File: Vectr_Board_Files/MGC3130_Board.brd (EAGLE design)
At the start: 146.5 x 107 mm, 112 parts, among them U101 MCP1755S, U102 MGC3130, U201 74HCT595BQ,115, U202 74HCT595BQ,115, U203 74HCT595BQ,115

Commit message: Preliminary Final Revision
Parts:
- moved R109 6.02 mm to (4.88, 53.9)
- flipped TO_MAIN to the bottom
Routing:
- net LED_PWM_4: track 236.8 -> 211.8 mm, vias 3 -> 4
- net GND: track 196.1 -> 217.4 mm, vias 11 -> 13
- net 5V: track 83.4 -> 99.9 mm
- net AGND: track 32.5 -> 48.0 mm
- net 3.3V: track 133.3 -> 120.3 mm
- net N$92: track 461.9 -> 473.4 mm, vias 17 -> 14
- net I2C1_SDA: track 103.4 -> 94.8 mm
- net LED_PWM_3: track 30.3 -> 38.7 mm, vias 0 -> 2
- net LED_PWM_1: track 63.8 -> 67.8 mm
- net MGC3130_IRQ: track 91.9 -> 94.8 mm, vias 0 -> 1
- net LED_PWM_2: track 82.4 -> 84.9 mm
- net SR_CLK: track 272.4 -> 270.4 mm, vias 7 -> 4
- net MGC3130_RESET: track 117.2 -> 115.3 mm
- net N$77: track 185.4 -> 187.2 mm
- net N$69: track 204.1 -> 205.8 mm
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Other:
- board text added: "VECTR HACKME ELECTRONICS REV 1.2"
- board text removed: "The connector is at 5.5 and 44.25"
- board text removed: "VECTR HACKME ELECTRONICS REV 1.1"

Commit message: Correcting the board files to match original production Vectr
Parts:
- TO_MAIN: value 16-SMT -> M50-3601042; device HackMe:16-SMT -> HackMe:M50-3601042
- moved R231 144.1 mm to (145.3, 8.08), flipped to the top
- moved R207 142.5 mm to (144.5, 102.0), flipped to the top
- moved T205 142.3 mm to (144.4, 4.74), flipped to the top
- moved C203 141.2 mm to (143.8, 17.6), flipped to the top
- moved T201 141.0 mm to (2.76, 92.4), flipped to the top
- moved C201 139.6 mm to (3.43, 11.9), flipped to the top
- moved R239 139.5 mm to (3.48, 60.0), flipped to the bottom
- moved R238 139.0 mm to (3.73, 75.4), flipped to the bottom
- moved R210 139.0 mm to (3.74, 68.0), flipped to the bottom
- moved R223 139.0 mm to (3.74, 44.8), flipped to the bottom
- moved R211 138.9 mm to (3.79, 83.5), flipped to the bottom
- moved R208 138.8 mm to (3.84, 36.7), flipped to the bottom
- moved R209 138.8 mm to (3.84, 52.4), flipped to the bottom
- moved R224 138.8 mm to (3.84, 29.3), flipped to the bottom
- moved R222 138.8 mm to (3.85, 21.5), flipped to the bottom
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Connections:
- net 5V: now also TO_MAIN.1, TO_MAIN.20; no longer TO_MAIN.P$1, TO_MAIN.P$2
- net AGND: now also TO_MAIN.11; no longer TO_MAIN.P$16
- net GND: now also TO_MAIN.10; no longer TO_MAIN.P$15
- net I2C1_SCL: now also TO_MAIN.2; no longer TO_MAIN.P$3
- net I2C1_SDA: now also TO_MAIN.19; no longer TO_MAIN.P$4
- net LED_PWM_1: now also TO_MAIN.5; no longer TO_MAIN.P$9
- net LED_PWM_2: now also TO_MAIN.16; no longer TO_MAIN.P$10
- net LED_PWM_3: now also TO_MAIN.6; no longer TO_MAIN.P$11
- net LED_PWM_4: now also TO_MAIN.15; no longer TO_MAIN.P$12
- net LED_PWM_5: now also TO_MAIN.7; no longer TO_MAIN.P$13
- net MGC3130_IRQ: now also TO_MAIN.18; no longer TO_MAIN.P$6
- net MGC3130_RESET: now also TO_MAIN.3; no longer TO_MAIN.P$5
- net SR_CLK: now also TO_MAIN.17; no longer TO_MAIN.P$8
- net SR_DATA: now also TO_MAIN.4; no longer TO_MAIN.P$7
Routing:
- net LED_PWM_4: track 211.8 -> 238.1 mm, vias 4 -> 3
- net GND: track 217.4 -> 197.9 mm, vias 13 -> 12
- net 3.3V: track 120.3 -> 133.3 mm
- net N$92: track 473.4 -> 461.9 mm, vias 14 -> 17
- net I2C1_SDA: track 94.8 -> 105.4 mm
- net 5V: track 99.9 -> 91.9 mm, vias 23 -> 25
- net LED_PWM_3: track 38.7 -> 32.0 mm, vias 2 -> 0
- net AGND: track 48.0 -> 42.1 mm
- net MGC3130_RESET: track 115.3 -> 118.6 mm
- net I2C1_SCL: track 110.1 -> 112.9 mm
- net LED_PWM_5: track 32.3 -> 35.1 mm
- net SR_CLK: track 270.4 -> 272.5 mm, vias 4 -> 7
- net LED_PWM_1: track 67.8 -> 65.7 mm
- net N$77: track 187.2 -> 185.4 mm
- net MGC3130_IRQ: track 94.8 -> 93.1 mm, vias 1 -> 0
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- added copper zone on layer 1, net AGND
- added copper zone on layer 16, net BOTTOM_RX
- added copper zone on layer 16, net CENTER_RX
- added copper zone on layer 16, net LEFT_RX
- added copper zone on layer 16, net RIGHT_RX
- added copper zone on layer 16, net TOP_RX
- removed copper zone on layer 16, net AGND
- removed copper zone on layer 1, net BOTTOM_RX
- removed copper zone on layer 1, net CENTER_RX
- removed copper zone on layer 1, net LEFT_RX
- removed copper zone on layer 1, net RIGHT_RX
- removed copper zone on layer 1, net TOP_RX
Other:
- board text added: "VECTR HACKME ELECTRONICS REV 1.1"
- board text removed: "VECTR HACKME ELECTRONICS REV 1.2"

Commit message: Null checking to find a bug.
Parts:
- moved R231 144.1 mm to (1.21, 8.08), flipped to the bottom
- moved R207 142.5 mm to (2.00, 102.0), flipped to the bottom
- moved T205 142.3 mm to (2.09, 4.74), flipped to the bottom
- moved C203 141.2 mm to (2.67, 17.6), flipped to the bottom
- moved T201 141.0 mm to (143.7, 92.4), flipped to the bottom
- moved C201 139.6 mm to (143.1, 11.9), flipped to the bottom
- moved R239 139.5 mm to (143.0, 60.0), flipped to the top
- moved R238 139.0 mm to (142.8, 75.4), flipped to the top
- moved R210 139.0 mm to (142.8, 68.0), flipped to the top
- moved R223 139.0 mm to (142.8, 44.8), flipped to the top
- moved R211 138.9 mm to (142.7, 83.5), flipped to the top
- moved R208 138.8 mm to (142.7, 36.7), flipped to the top
- moved R209 138.8 mm to (142.7, 52.4), flipped to the top
- moved R224 138.8 mm to (142.7, 29.3), flipped to the top
- moved R222 138.8 mm to (142.7, 21.5), flipped to the top
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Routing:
- added copper zone on layer 16, net AGND
- added copper zone on layer 1, net BOTTOM_RX
- added copper zone on layer 1, net CENTER_RX
- added copper zone on layer 1, net LEFT_RX
- added copper zone on layer 1, net RIGHT_RX
- added copper zone on layer 1, net TOP_RX
- removed copper zone on layer 1, net AGND
- removed copper zone on layer 16, net BOTTOM_RX
- removed copper zone on layer 16, net CENTER_RX
- removed copper zone on layer 16, net LEFT_RX
- removed copper zone on layer 16, net RIGHT_RX
- removed copper zone on layer 16, net TOP_RX

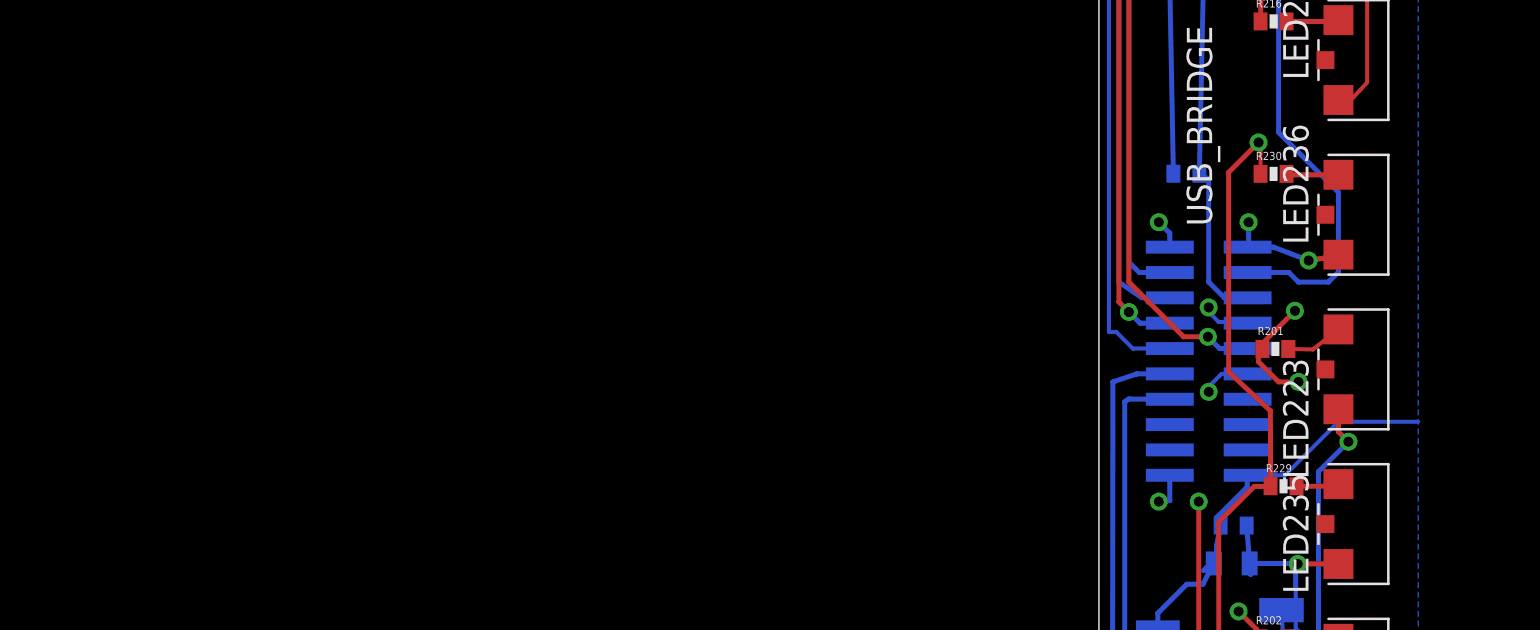
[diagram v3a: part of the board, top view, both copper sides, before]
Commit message: Changing connectors
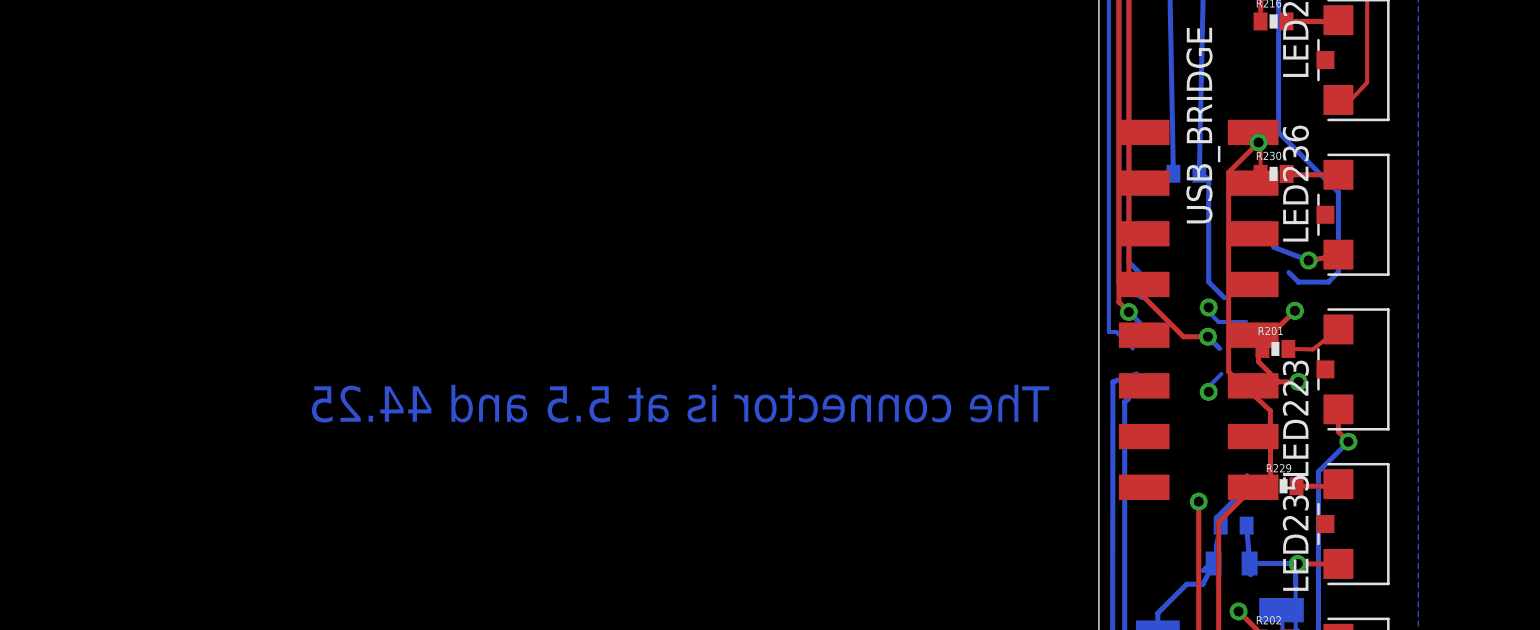
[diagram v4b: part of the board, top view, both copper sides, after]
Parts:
- TO_MAIN: value M50-3601042 -> 16-SMT; device HackMe:M50-3601042 -> HackMe:16-SMT
- moved TO_MAIN 5.77 mm to (5.00, 50.0)
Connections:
- net 5V: now also TO_MAIN.P$1, TO_MAIN.P$2; no longer TO_MAIN.1, TO_MAIN.20
- net AGND: now also TO_MAIN.P$16; no longer TO_MAIN.11
- net GND: now also TO_MAIN.P$15; no longer TO_MAIN.10
- net I2C1_SCL: now also TO_MAIN.P$3; no longer TO_MAIN.2
- net I2C1_SDA: now also TO_MAIN.P$4; no longer TO_MAIN.19
- net LED_PWM_1: now also TO_MAIN.P$9; no longer TO_MAIN.5
- net LED_PWM_2: now also TO_MAIN.P$10; no longer TO_MAIN.16
- net LED_PWM_3: now also TO_MAIN.P$11; no longer TO_MAIN.6
- net LED_PWM_4: now also TO_MAIN.P$12; no longer TO_MAIN.15
- net LED_PWM_5: now also TO_MAIN.P$13; no longer TO_MAIN.7
- net MGC3130_IRQ: now also TO_MAIN.P$6; no longer TO_MAIN.18
- net MGC3130_RESET: now also TO_MAIN.P$5; no longer TO_MAIN.3
- net SR_CLK: now also TO_MAIN.P$8; no longer TO_MAIN.17
- net SR_DATA: now also TO_MAIN.P$7; no longer TO_MAIN.4
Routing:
- net AGND: track 42.1 -> 32.5 mm
- net 5V: track 91.9 -> 83.4 mm, vias 25 -> 23
- net I2C1_SDA: track 105.4 -> 103.4 mm
- net LED_PWM_5: track 35.1 -> 33.0 mm
- net LED_PWM_1: track 65.7 -> 63.8 mm
- net GND: track 197.9 -> 196.1 mm, vias 12 -> 11
- net LED_PWM_3: track 32.0 -> 30.3 mm
- net I2C1_SCL: track 112.9 -> 111.4 mm
- net SR_DATA: track 56.4 -> 54.9 mm
- net MGC3130_RESET: track 118.6 -> 117.2 mm
- net LED_PWM_2: track 83.8 -> 82.4 mm
- net LED_PWM_4: track 238.1 -> 236.8 mm
- net MGC3130_IRQ: track 93.1 -> 91.9 mm
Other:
- board text added: "The connector is at 5.5 and 44.25"
